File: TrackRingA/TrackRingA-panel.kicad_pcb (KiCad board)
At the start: 2 copper layers, 81 x 81 mm, 350 parts, among them J1 Conn_01x04, U1 TLV493D-A1B6, U2 LIS2DTW12

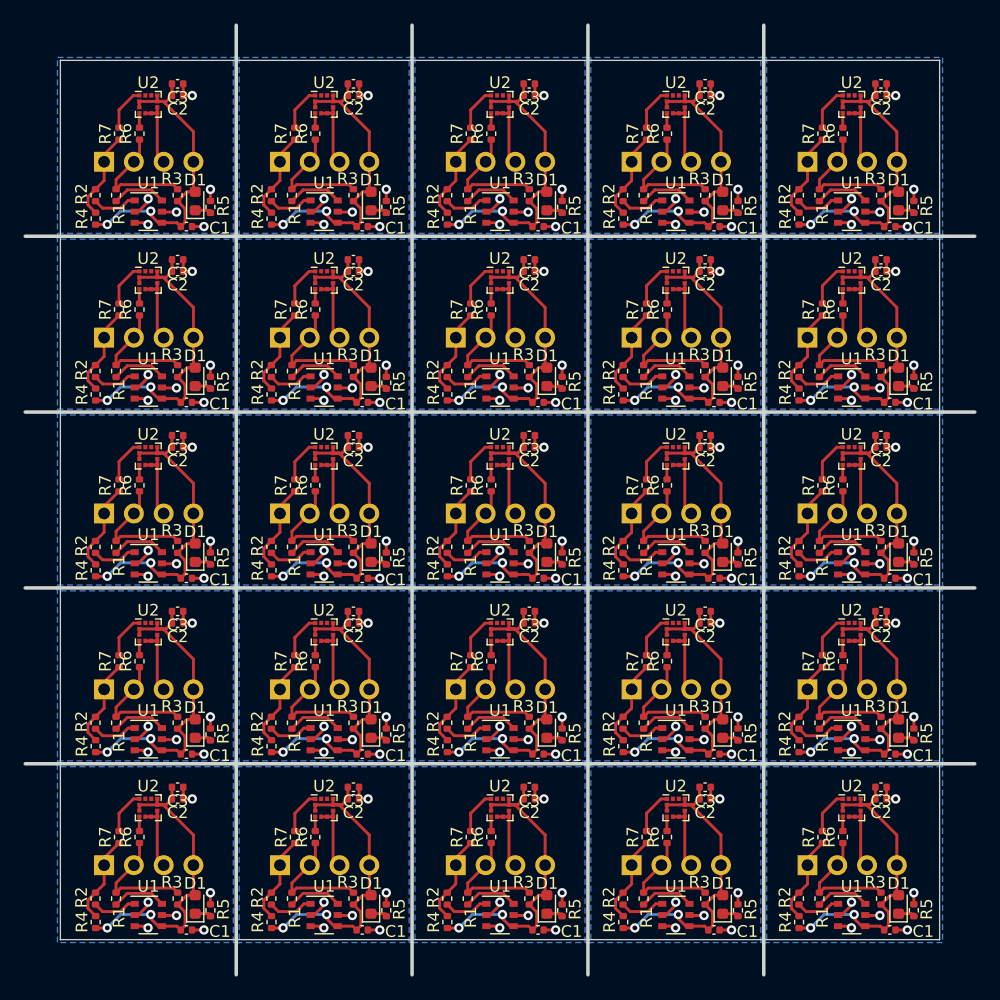
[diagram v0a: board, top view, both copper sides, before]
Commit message: Finished BusChain1.1 and added power daisy-chaining option
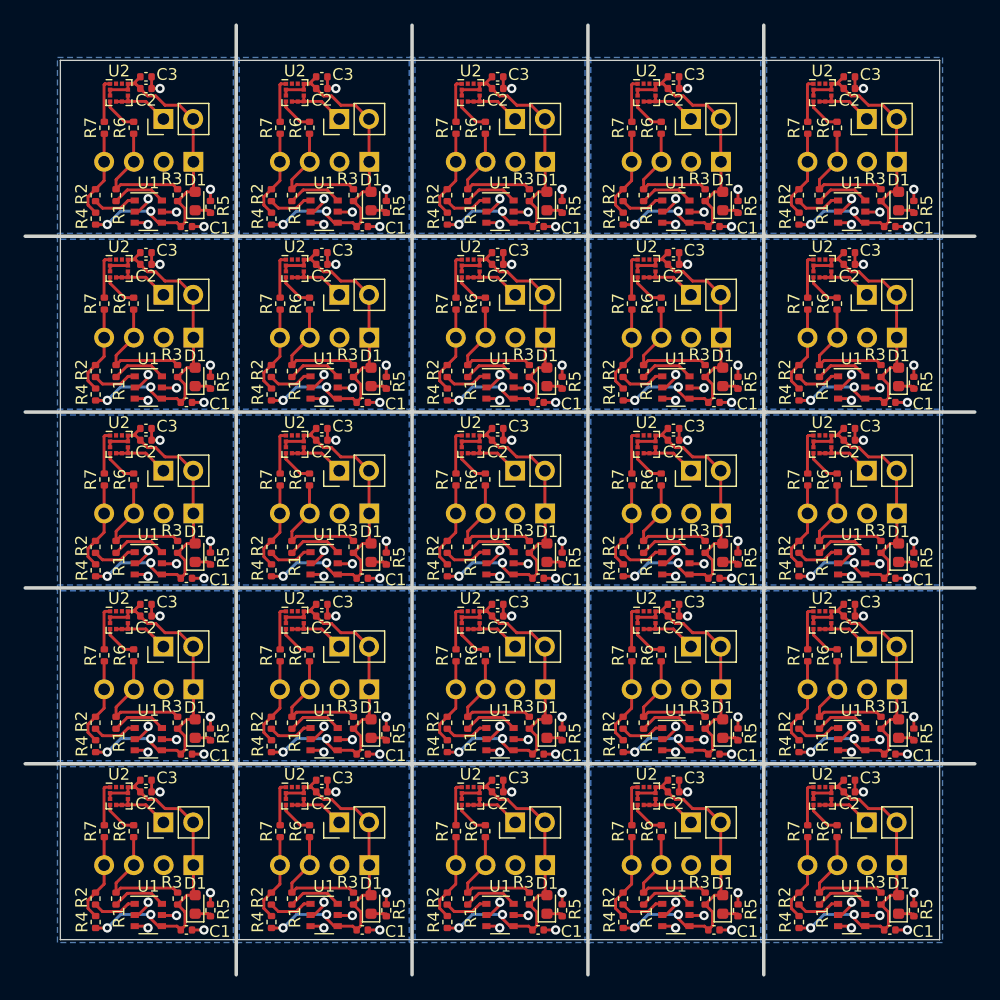
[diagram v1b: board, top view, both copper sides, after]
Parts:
- removed the C2 at (121.0, 53.0)
- removed the C2 at (166.0, 53.0)
- removed the C2 at (136.0, 23.0)
- removed the C2 at (166.0, 68.0)
- removed the C2 at (181.0, 68.0)
- removed the C2 at (136.0, 53.0)
- removed the C2 at (151.0, 23.0)
- removed the C2 at (166.0, 38.0)
- removed the C2 at (166.0, 83.0)
- removed the C2 at (151.0, 68.0)
- removed the C2 at (181.0, 38.0)
- removed the C2 at (181.0, 23.0)
- removed the C2 at (121.0, 38.0)
- removed the C2 at (151.0, 83.0)
- removed the C2 at (136.0, 38.0)
- removed the C2 at (121.0, 68.0)
- removed the C2 at (136.0, 83.0)
- removed the C2 at (151.0, 53.0)
- removed the C2 at (166.0, 23.0)
- removed the C2 at (181.0, 83.0)
- removed the C2 at (136.0, 68.0)
- removed the C2 at (151.0, 38.0)
- removed the C2 at (121.0, 83.0)
- removed the C2 at (181.0, 53.0)
- removed the C3 at (181.0, 22.0)
- removed the C3 at (166.0, 37.0)
- removed the C3 at (121.0, 67.0)
- removed the C3 at (136.0, 82.0)
- removed the C3 at (181.0, 67.0)
- removed the C3 at (136.0, 52.0)
- removed the C3 at (121.0, 22.0)
- removed the C3 at (136.0, 67.0)
- removed the C3 at (151.0, 37.0)
- removed the C3 at (151.0, 82.0)
- removed the C3 at (121.0, 82.0)
- removed the C3 at (181.0, 82.0)
- removed the C3 at (121.0, 37.0)
- removed the C3 at (151.0, 22.0)
- removed the C3 at (166.0, 52.0)
- removed the C3 at (121.0, 52.0)
- removed the C3 at (166.0, 82.0)
- removed the C3 at (181.0, 37.0)
- removed the C3 at (151.0, 52.0)
- removed the C3 at (181.0, 52.0)
- removed the C3 at (166.0, 67.0)
- removed the C3 at (136.0, 37.0)
- removed the C3 at (151.0, 67.0)
- removed the C3 at (136.0, 22.0)
- removed the J1 at (174.7, 58.6)
- removed the J1 at (144.7, 43.6)
- removed the J1 at (144.7, 28.6)
- removed the J1 at (129.7, 73.7)
- removed the J1 at (159.7, 43.6)
- removed the J1 at (114.7, 88.7)
- removed the J1 at (174.7, 88.7)
- removed the J1 at (174.7, 43.6)
- removed the J1 at (144.7, 88.7)
- removed the J1 at (159.7, 88.7)
- removed the J1 at (144.7, 73.7)
- removed the J1 at (159.7, 28.6)
- removed the J1 at (129.7, 28.6)
- removed the J1 at (114.7, 28.6)
- removed the J1 at (159.7, 73.7)
- removed the J1 at (144.7, 58.6)
- removed the J1 at (114.7, 43.6)
- removed the J1 at (114.7, 58.6)
- removed the J1 at (159.7, 58.6)
- removed the J1 at (129.7, 58.6)
- removed the J1 at (114.7, 73.7)
- removed the J1 at (174.7, 73.7)
- removed the J1 at (129.7, 43.6)
- removed the J1 at (129.7, 88.7)
- removed the J1 at (174.7, 28.6)
- removed the R6 at (177.8, 26.2)
- removed the R6 at (162.8, 86.2)
- removed the R6 at (117.8, 71.2)
- removed the R6 at (132.8, 71.2)
- removed the R6 at (162.8, 71.2)
- removed the R6 at (147.8, 86.2)
- removed the R6 at (177.8, 71.2)
- removed the R6 at (147.8, 26.2)
- removed the R6 at (132.8, 41.2)
- removed the R6 at (147.8, 71.2)
- removed the R6 at (132.8, 86.2)
- removed the R6 at (132.8, 56.2)
- removed the R6 at (177.8, 86.2)
- removed the R6 at (147.8, 56.2)
- removed the R6 at (162.8, 26.2)
- removed the R6 at (162.8, 56.2)
- removed the R6 at (117.8, 56.2)
- removed the R6 at (117.8, 86.2)
- removed the R6 at (177.8, 41.2)
- removed the R6 at (147.8, 41.2)
- removed the R6 at (117.8, 26.2)
- removed the R6 at (177.8, 56.2)
- removed the R6 at (117.8, 41.2)
- removed the R6 at (162.8, 41.2)
- removed the R7 at (131.0, 86.2)
- removed the R7 at (176.0, 71.2)
- removed the R7 at (176.0, 41.2)
- removed the R7 at (131.0, 71.2)
- removed the R7 at (161.0, 86.2)
- removed the R7 at (161.0, 26.2)
- removed the R7 at (161.0, 56.2)
- removed the R7 at (116.0, 26.2)
- removed the R7 at (146.0, 56.2)
- removed the R7 at (146.0, 86.2)
- removed the R7 at (131.0, 41.2)
- removed the R7 at (176.0, 86.2)
- removed the R7 at (131.0, 56.2)
- removed the R7 at (161.0, 41.2)
- removed the R7 at (176.0, 56.2)
- removed the R7 at (116.0, 86.2)
- removed the R7 at (116.0, 71.2)
- removed the R7 at (146.0, 41.2)
- removed the R7 at (146.0, 71.2)
- removed the R7 at (116.0, 41.2)
- removed the R7 at (116.0, 56.2)
- removed the R7 at (146.0, 26.2)
- removed the R7 at (161.0, 71.2)
- removed the R7 at (176.0, 26.2)
- removed the U2 at (118.5, 83.8)
- removed the U2 at (163.5, 68.8)
- removed the U2 at (133.5, 83.8)
- removed the U2 at (163.5, 38.8)
- removed the U2 at (148.5, 38.8)
- removed the U2 at (163.5, 23.8)
- removed the U2 at (133.5, 38.8)
- removed the U2 at (118.5, 68.8)
- removed the U2 at (148.5, 83.8)
- removed the U2 at (118.5, 38.8)
- removed the U2 at (118.5, 53.8)
- removed the U2 at (163.5, 83.8)
- removed the U2 at (133.5, 53.8)
- removed the U2 at (148.5, 53.8)
- removed the U2 at (178.5, 23.8)
- removed the U2 at (178.5, 68.8)
- removed the U2 at (148.5, 23.8)
- removed the U2 at (178.5, 38.8)
- removed the U2 at (148.5, 68.8)
- removed the U2 at (178.5, 83.8)
- removed the U2 at (133.5, 68.8)
- removed the U2 at (163.5, 53.8)
- removed the U2 at (178.5, 53.8)
- removed the U2 at (133.5, 23.8)
- added C2: 0.1uF, Capacitor_SMD:C_0402_1005Metric, F.Cu at (118.3, 67.4)
- added C2: 0.1uF, Capacitor_SMD:C_0402_1005Metric, F.Cu at (148.3, 37.4)
- added C2: 0.1uF, Capacitor_SMD:C_0402_1005Metric, F.Cu at (163.3, 82.4)
- added C2: 0.1uF, Capacitor_SMD:C_0402_1005Metric, F.Cu at (133.3, 37.4)
- added C2: 0.1uF, Capacitor_SMD:C_0402_1005Metric, F.Cu at (163.3, 67.4)
- added C2: 0.1uF, Capacitor_SMD:C_0402_1005Metric, F.Cu at (148.3, 67.4)
- added C2: 0.1uF, Capacitor_SMD:C_0402_1005Metric, F.Cu at (178.3, 67.4)
- added C2: 0.1uF, Capacitor_SMD:C_0402_1005Metric, F.Cu at (178.3, 37.4)
- added C2: 0.1uF, Capacitor_SMD:C_0402_1005Metric, F.Cu at (178.3, 22.4)
- added C2: 0.1uF, Capacitor_SMD:C_0402_1005Metric, F.Cu at (178.3, 52.4)
- added C2: 0.1uF, Capacitor_SMD:C_0402_1005Metric, F.Cu at (163.3, 37.4)
- added C2: 0.1uF, Capacitor_SMD:C_0402_1005Metric, F.Cu at (163.3, 22.4)
- added C2: 0.1uF, Capacitor_SMD:C_0402_1005Metric, F.Cu at (163.3, 52.4)
- added C2: 0.1uF, Capacitor_SMD:C_0402_1005Metric, F.Cu at (133.3, 82.4)
- added C2: 0.1uF, Capacitor_SMD:C_0402_1005Metric, F.Cu at (118.3, 52.4)
- added C2: 0.1uF, Capacitor_SMD:C_0402_1005Metric, F.Cu at (133.3, 22.4)
- added C2: 0.1uF, Capacitor_SMD:C_0402_1005Metric, F.Cu at (148.3, 82.4)
- added C2: 0.1uF, Capacitor_SMD:C_0402_1005Metric, F.Cu at (178.3, 82.4)
- added C2: 0.1uF, Capacitor_SMD:C_0402_1005Metric, F.Cu at (133.3, 67.4)
- added C2: 0.1uF, Capacitor_SMD:C_0402_1005Metric, F.Cu at (133.3, 52.4)
- added C2: 0.1uF, Capacitor_SMD:C_0402_1005Metric, F.Cu at (118.3, 22.4)
- added C2: 0.1uF, Capacitor_SMD:C_0402_1005Metric, F.Cu at (118.3, 37.4)
- added C2: 0.1uF, Capacitor_SMD:C_0402_1005Metric, F.Cu at (148.3, 52.4)
- added C2: 0.1uF, Capacitor_SMD:C_0402_1005Metric, F.Cu at (118.3, 82.4)
- added C3: 0.1uF, Capacitor_SMD:C_0402_1005Metric, F.Cu at (163.3, 66.4)
- added C3: 0.1uF, Capacitor_SMD:C_0402_1005Metric, F.Cu at (118.3, 36.4)
- added C3: 0.1uF, Capacitor_SMD:C_0402_1005Metric, F.Cu at (178.3, 36.4)
- added C3: 0.1uF, Capacitor_SMD:C_0402_1005Metric, F.Cu at (133.3, 51.4)
- added C3: 0.1uF, Capacitor_SMD:C_0402_1005Metric, F.Cu at (118.3, 21.4)
- added C3: 0.1uF, Capacitor_SMD:C_0402_1005Metric, F.Cu at (163.3, 51.4)
- added C3: 0.1uF, Capacitor_SMD:C_0402_1005Metric, F.Cu at (178.3, 51.4)
- added C3: 0.1uF, Capacitor_SMD:C_0402_1005Metric, F.Cu at (148.3, 66.4)
- added C3: 0.1uF, Capacitor_SMD:C_0402_1005Metric, F.Cu at (178.3, 21.4)
- added C3: 0.1uF, Capacitor_SMD:C_0402_1005Metric, F.Cu at (178.3, 81.4)
- added C3: 0.1uF, Capacitor_SMD:C_0402_1005Metric, F.Cu at (133.3, 81.4)
- added C3: 0.1uF, Capacitor_SMD:C_0402_1005Metric, F.Cu at (148.3, 21.4)
- added C3: 0.1uF, Capacitor_SMD:C_0402_1005Metric, F.Cu at (163.3, 21.4)
- added C3: 0.1uF, Capacitor_SMD:C_0402_1005Metric, F.Cu at (118.3, 51.4)
- added C3: 0.1uF, Capacitor_SMD:C_0402_1005Metric, F.Cu at (118.3, 81.4)
- added C3: 0.1uF, Capacitor_SMD:C_0402_1005Metric, F.Cu at (178.3, 66.4)
- added C3: 0.1uF, Capacitor_SMD:C_0402_1005Metric, F.Cu at (163.3, 36.4)
- added C3: 0.1uF, Capacitor_SMD:C_0402_1005Metric, F.Cu at (148.3, 81.4)
- added C3: 0.1uF, Capacitor_SMD:C_0402_1005Metric, F.Cu at (133.3, 66.4)
- added C3: 0.1uF, Capacitor_SMD:C_0402_1005Metric, F.Cu at (118.3, 66.4)
- added C3: 0.1uF, Capacitor_SMD:C_0402_1005Metric, F.Cu at (148.3, 36.4)
- added C3: 0.1uF, Capacitor_SMD:C_0402_1005Metric, F.Cu at (133.3, 21.4)
- added C3: 0.1uF, Capacitor_SMD:C_0402_1005Metric, F.Cu at (148.3, 51.4)
- added C3: 0.1uF, Capacitor_SMD:C_0402_1005Metric, F.Cu at (163.3, 81.4)
- added J1: Conn_01x04, Connector_PinHeader_2.54mm:PinHeader_1x04_P2.54mm_Vertical, B.Cu at (137.3, 43.6)
- added J1: Conn_01x04, Connector_PinHeader_2.54mm:PinHeader_1x04_P2.54mm_Vertical, B.Cu at (167.3, 43.6)
- added J1: Conn_01x04, Connector_PinHeader_2.54mm:PinHeader_1x04_P2.54mm_Vertical, B.Cu at (182.3, 28.6)
- added J1: Conn_01x04, Connector_PinHeader_2.54mm:PinHeader_1x04_P2.54mm_Vertical, B.Cu at (152.3, 28.6)
- added J1: Conn_01x04, Connector_PinHeader_2.54mm:PinHeader_1x04_P2.54mm_Vertical, B.Cu at (152.3, 58.6)
- added J1: Conn_01x04, Connector_PinHeader_2.54mm:PinHeader_1x04_P2.54mm_Vertical, B.Cu at (152.3, 43.6)
- added J1: Conn_01x04, Connector_PinHeader_2.54mm:PinHeader_1x04_P2.54mm_Vertical, B.Cu at (137.3, 88.7)
- added J1: Conn_01x04, Connector_PinHeader_2.54mm:PinHeader_1x04_P2.54mm_Vertical, B.Cu at (167.3, 88.7)
- added J1: Conn_01x04, Connector_PinHeader_2.54mm:PinHeader_1x04_P2.54mm_Vertical, B.Cu at (122.3, 58.6)
- added J1: Conn_01x04, Connector_PinHeader_2.54mm:PinHeader_1x04_P2.54mm_Vertical, B.Cu at (182.3, 58.6)
- added J1: Conn_01x04, Connector_PinHeader_2.54mm:PinHeader_1x04_P2.54mm_Vertical, B.Cu at (122.3, 28.6)
- added J1: Conn_01x04, Connector_PinHeader_2.54mm:PinHeader_1x04_P2.54mm_Vertical, B.Cu at (182.3, 43.6)
- added J1: Conn_01x04, Connector_PinHeader_2.54mm:PinHeader_1x04_P2.54mm_Vertical, B.Cu at (167.3, 73.7)
- added J1: Conn_01x04, Connector_PinHeader_2.54mm:PinHeader_1x04_P2.54mm_Vertical, B.Cu at (137.3, 73.7)
- added J1: Conn_01x04, Connector_PinHeader_2.54mm:PinHeader_1x04_P2.54mm_Vertical, B.Cu at (182.3, 88.7)
- added J1: Conn_01x04, Connector_PinHeader_2.54mm:PinHeader_1x04_P2.54mm_Vertical, B.Cu at (137.3, 28.6)
- added J1: Conn_01x04, Connector_PinHeader_2.54mm:PinHeader_1x04_P2.54mm_Vertical, B.Cu at (137.3, 58.6)
- added J1: Conn_01x04, Connector_PinHeader_2.54mm:PinHeader_1x04_P2.54mm_Vertical, B.Cu at (167.3, 28.6)
- added J1: Conn_01x04, Connector_PinHeader_2.54mm:PinHeader_1x04_P2.54mm_Vertical, B.Cu at (122.3, 43.6)
- added J1: Conn_01x04, Connector_PinHeader_2.54mm:PinHeader_1x04_P2.54mm_Vertical, B.Cu at (122.3, 73.7)
- added J1: Conn_01x04, Connector_PinHeader_2.54mm:PinHeader_1x04_P2.54mm_Vertical, B.Cu at (152.3, 88.7)
- added J1: Conn_01x04, Connector_PinHeader_2.54mm:PinHeader_1x04_P2.54mm_Vertical, B.Cu at (152.3, 73.7)
- added J1: Conn_01x04, Connector_PinHeader_2.54mm:PinHeader_1x04_P2.54mm_Vertical, B.Cu at (122.3, 88.7)
- added J1: Conn_01x04, Connector_PinHeader_2.54mm:PinHeader_1x04_P2.54mm_Vertical, B.Cu at (167.3, 58.6)
- added J1: Conn_01x04, Connector_PinHeader_2.54mm:PinHeader_1x04_P2.54mm_Vertical, B.Cu at (182.3, 73.7)
- added J2: Conn_01x02, Connector_PinHeader_2.54mm:PinHeader_1x02_P2.54mm_Vertical, F.Cu at (164.8, 40.0)
- added J2: Conn_01x02, Connector_PinHeader_2.54mm:PinHeader_1x02_P2.54mm_Vertical, F.Cu at (134.8, 85.0)
- added J2: Conn_01x02, Connector_PinHeader_2.54mm:PinHeader_1x02_P2.54mm_Vertical, F.Cu at (119.8, 55.0)
- added J2: Conn_01x02, Connector_PinHeader_2.54mm:PinHeader_1x02_P2.54mm_Vertical, F.Cu at (149.8, 85.0)
- added J2: Conn_01x02, Connector_PinHeader_2.54mm:PinHeader_1x02_P2.54mm_Vertical, F.Cu at (179.8, 85.0)
- added J2: Conn_01x02, Connector_PinHeader_2.54mm:PinHeader_1x02_P2.54mm_Vertical, F.Cu at (149.8, 25.0)
- added J2: Conn_01x02, Connector_PinHeader_2.54mm:PinHeader_1x02_P2.54mm_Vertical, F.Cu at (134.8, 40.0)
- added J2: Conn_01x02, Connector_PinHeader_2.54mm:PinHeader_1x02_P2.54mm_Vertical, F.Cu at (164.8, 25.0)
- added J2: Conn_01x02, Connector_PinHeader_2.54mm:PinHeader_1x02_P2.54mm_Vertical, F.Cu at (134.8, 70.0)
- added J2: Conn_01x02, Connector_PinHeader_2.54mm:PinHeader_1x02_P2.54mm_Vertical, F.Cu at (134.8, 25.0)
- added J2: Conn_01x02, Connector_PinHeader_2.54mm:PinHeader_1x02_P2.54mm_Vertical, F.Cu at (179.8, 40.0)
- added J2: Conn_01x02, Connector_PinHeader_2.54mm:PinHeader_1x02_P2.54mm_Vertical, F.Cu at (179.8, 70.0)
- added J2: Conn_01x02, Connector_PinHeader_2.54mm:PinHeader_1x02_P2.54mm_Vertical, F.Cu at (149.8, 40.0)
- added J2: Conn_01x02, Connector_PinHeader_2.54mm:PinHeader_1x02_P2.54mm_Vertical, F.Cu at (119.8, 70.0)
- added J2: Conn_01x02, Connector_PinHeader_2.54mm:PinHeader_1x02_P2.54mm_Vertical, F.Cu at (164.8, 85.0)
- added J2: Conn_01x02, Connector_PinHeader_2.54mm:PinHeader_1x02_P2.54mm_Vertical, F.Cu at (149.8, 70.0)
- added J2: Conn_01x02, Connector_PinHeader_2.54mm:PinHeader_1x02_P2.54mm_Vertical, F.Cu at (179.8, 25.0)
- added J2: Conn_01x02, Connector_PinHeader_2.54mm:PinHeader_1x02_P2.54mm_Vertical, F.Cu at (119.8, 25.0)
- added J2: Conn_01x02, Connector_PinHeader_2.54mm:PinHeader_1x02_P2.54mm_Vertical, F.Cu at (164.8, 55.0)
- added J2: Conn_01x02, Connector_PinHeader_2.54mm:PinHeader_1x02_P2.54mm_Vertical, F.Cu at (179.8, 55.0)
- added J2: Conn_01x02, Connector_PinHeader_2.54mm:PinHeader_1x02_P2.54mm_Vertical, F.Cu at (134.8, 55.0)
- added J2: Conn_01x02, Connector_PinHeader_2.54mm:PinHeader_1x02_P2.54mm_Vertical, F.Cu at (119.8, 40.0)
- added J2: Conn_01x02, Connector_PinHeader_2.54mm:PinHeader_1x02_P2.54mm_Vertical, F.Cu at (149.8, 55.0)
- added J2: Conn_01x02, Connector_PinHeader_2.54mm:PinHeader_1x02_P2.54mm_Vertical, F.Cu at (164.8, 70.0)
- added J2: Conn_01x02, Connector_PinHeader_2.54mm:PinHeader_1x02_P2.54mm_Vertical, F.Cu at (119.8, 85.0)
- added R6: 100, Resistor_SMD:R_0402_1005Metric, F.Cu at (162.2, 55.8)
- added R6: 100, Resistor_SMD:R_0402_1005Metric, F.Cu at (177.2, 40.8)
- added R6: 100, Resistor_SMD:R_0402_1005Metric, F.Cu at (177.2, 55.8)
- added R6: 100, Resistor_SMD:R_0402_1005Metric, F.Cu at (162.2, 25.8)
- added R6: 100, Resistor_SMD:R_0402_1005Metric, F.Cu at (177.2, 85.8)
- added R6: 100, Resistor_SMD:R_0402_1005Metric, F.Cu at (147.2, 25.8)
- added R6: 100, Resistor_SMD:R_0402_1005Metric, F.Cu at (147.2, 40.8)
- added R6: 100, Resistor_SMD:R_0402_1005Metric, F.Cu at (117.2, 85.8)
- added R6: 100, Resistor_SMD:R_0402_1005Metric, F.Cu at (162.2, 40.8)
- added R6: 100, Resistor_SMD:R_0402_1005Metric, F.Cu at (117.2, 55.8)
- added R6: 100, Resistor_SMD:R_0402_1005Metric, F.Cu at (162.2, 70.8)
- added R6: 100, Resistor_SMD:R_0402_1005Metric, F.Cu at (132.2, 85.8)
- added R6: 100, Resistor_SMD:R_0402_1005Metric, F.Cu at (132.2, 40.8)
- added R6: 100, Resistor_SMD:R_0402_1005Metric, F.Cu at (177.2, 25.8)
- added R6: 100, Resistor_SMD:R_0402_1005Metric, F.Cu at (162.2, 85.8)
- added R6: 100, Resistor_SMD:R_0402_1005Metric, F.Cu at (177.2, 70.8)
- added R6: 100, Resistor_SMD:R_0402_1005Metric, F.Cu at (147.2, 70.8)
- added R6: 100, Resistor_SMD:R_0402_1005Metric, F.Cu at (117.2, 70.8)
- added R6: 100, Resistor_SMD:R_0402_1005Metric, F.Cu at (117.2, 40.8)
- added R6: 100, Resistor_SMD:R_0402_1005Metric, F.Cu at (147.2, 55.8)
- added R6: 100, Resistor_SMD:R_0402_1005Metric, F.Cu at (117.2, 25.8)
- added R6: 100, Resistor_SMD:R_0402_1005Metric, F.Cu at (147.2, 85.8)
- added R6: 100, Resistor_SMD:R_0402_1005Metric, F.Cu at (132.2, 70.8)
- added R6: 100, Resistor_SMD:R_0402_1005Metric, F.Cu at (132.2, 55.8)
- added R7: 100, Resistor_SMD:R_0402_1005Metric, F.Cu at (129.8, 70.8)
- added R7: 100, Resistor_SMD:R_0402_1005Metric, F.Cu at (129.8, 25.8)
- added R7: 100, Resistor_SMD:R_0402_1005Metric, F.Cu at (144.8, 25.8)
- added R7: 100, Resistor_SMD:R_0402_1005Metric, F.Cu at (129.8, 40.8)
- added R7: 100, Resistor_SMD:R_0402_1005Metric, F.Cu at (174.8, 70.8)
- added R7: 100, Resistor_SMD:R_0402_1005Metric, F.Cu at (159.8, 70.8)
- added R7: 100, Resistor_SMD:R_0402_1005Metric, F.Cu at (144.8, 55.8)
- added R7: 100, Resistor_SMD:R_0402_1005Metric, F.Cu at (114.8, 70.8)
- added R7: 100, Resistor_SMD:R_0402_1005Metric, F.Cu at (144.8, 40.8)
- added R7: 100, Resistor_SMD:R_0402_1005Metric, F.Cu at (129.8, 85.8)
- added R7: 100, Resistor_SMD:R_0402_1005Metric, F.Cu at (159.8, 55.8)
- added R7: 100, Resistor_SMD:R_0402_1005Metric, F.Cu at (129.8, 55.8)
- added R7: 100, Resistor_SMD:R_0402_1005Metric, F.Cu at (174.8, 40.8)
- added R7: 100, Resistor_SMD:R_0402_1005Metric, F.Cu at (114.8, 40.8)
- added R7: 100, Resistor_SMD:R_0402_1005Metric, F.Cu at (174.8, 25.8)
- added R7: 100, Resistor_SMD:R_0402_1005Metric, F.Cu at (159.8, 85.8)
- added R7: 100, Resistor_SMD:R_0402_1005Metric, F.Cu at (114.8, 55.8)
- added R7: 100, Resistor_SMD:R_0402_1005Metric, F.Cu at (144.8, 70.8)
- added R7: 100, Resistor_SMD:R_0402_1005Metric, F.Cu at (159.8, 40.8)
- added R7: 100, Resistor_SMD:R_0402_1005Metric, F.Cu at (174.8, 85.8)
- added R7: 100, Resistor_SMD:R_0402_1005Metric, F.Cu at (114.8, 85.8)
- added R7: 100, Resistor_SMD:R_0402_1005Metric, F.Cu at (144.8, 85.8)
- added R7: 100, Resistor_SMD:R_0402_1005Metric, F.Cu at (174.8, 55.8)
- added R7: 100, Resistor_SMD:R_0402_1005Metric, F.Cu at (114.8, 25.8)
- added U2: LIS2DTW12, Package_LGA:LGA-12_2x2mm_P0.5mm, F.Cu at (161.0, 82.8)
- added U2: LIS2DTW12, Package_LGA:LGA-12_2x2mm_P0.5mm, F.Cu at (131.0, 37.8)
- added U2: LIS2DTW12, Package_LGA:LGA-12_2x2mm_P0.5mm, F.Cu at (131.0, 22.8)
- added U2: LIS2DTW12, Package_LGA:LGA-12_2x2mm_P0.5mm, F.Cu at (161.0, 22.8)
- added U2: LIS2DTW12, Package_LGA:LGA-12_2x2mm_P0.5mm, F.Cu at (116.0, 82.8)
- added U2: LIS2DTW12, Package_LGA:LGA-12_2x2mm_P0.5mm, F.Cu at (146.0, 67.8)
- added U2: LIS2DTW12, Package_LGA:LGA-12_2x2mm_P0.5mm, F.Cu at (161.0, 52.8)
- added U2: LIS2DTW12, Package_LGA:LGA-12_2x2mm_P0.5mm, F.Cu at (176.0, 52.8)
- added U2: LIS2DTW12, Package_LGA:LGA-12_2x2mm_P0.5mm, F.Cu at (176.0, 67.8)
- added U2: LIS2DTW12, Package_LGA:LGA-12_2x2mm_P0.5mm, F.Cu at (131.0, 67.8)
- added U2: LIS2DTW12, Package_LGA:LGA-12_2x2mm_P0.5mm, F.Cu at (131.0, 82.8)
- added U2: LIS2DTW12, Package_LGA:LGA-12_2x2mm_P0.5mm, F.Cu at (161.0, 37.8)
- added U2: LIS2DTW12, Package_LGA:LGA-12_2x2mm_P0.5mm, F.Cu at (176.0, 82.8)
- added U2: LIS2DTW12, Package_LGA:LGA-12_2x2mm_P0.5mm, F.Cu at (116.0, 67.8)
- added U2: LIS2DTW12, Package_LGA:LGA-12_2x2mm_P0.5mm, F.Cu at (116.0, 22.8)
- added U2: LIS2DTW12, Package_LGA:LGA-12_2x2mm_P0.5mm, F.Cu at (116.0, 52.8)
- added U2: LIS2DTW12, Package_LGA:LGA-12_2x2mm_P0.5mm, F.Cu at (116.0, 37.8)
- added U2: LIS2DTW12, Package_LGA:LGA-12_2x2mm_P0.5mm, F.Cu at (146.0, 37.8)
- added U2: LIS2DTW12, Package_LGA:LGA-12_2x2mm_P0.5mm, F.Cu at (176.0, 37.8)
- added U2: LIS2DTW12, Package_LGA:LGA-12_2x2mm_P0.5mm, F.Cu at (146.0, 52.8)
- added U2: LIS2DTW12, Package_LGA:LGA-12_2x2mm_P0.5mm, F.Cu at (146.0, 82.8)
- added U2: LIS2DTW12, Package_LGA:LGA-12_2x2mm_P0.5mm, F.Cu at (161.0, 67.8)
- added U2: LIS2DTW12, Package_LGA:LGA-12_2x2mm_P0.5mm, F.Cu at (131.0, 52.8)
- added U2: LIS2DTW12, Package_LGA:LGA-12_2x2mm_P0.5mm, F.Cu at (176.0, 22.8)
- moved R3 60.0 mm to (181.0, 91.5)
- moved R3 60.0 mm to (181.0, 31.5)
- moved R1 45.0 mm to (115.8, 31.5)
- moved R1 45.0 mm to (160.8, 31.5)
- moved C3 35.7 mm to (133.3, 36.4)
- moved R7 28.8 mm to (159.8, 25.8)
- moved U2 27.5 mm to (146.0, 22.8)
- moved C2 27.3 mm to (148.3, 22.4)
- moved D1 15.0 mm to (137.5, 32.0)
- moved D1 15.0 mm to (122.5, 32.0)
- moved R2 15.0 mm to (114.0, 31.5)
- moved R2 15.0 mm to (129.0, 31.5)
- moved R4 15.0 mm to (159.0, 33.5)
- moved R4 15.0 mm to (174.0, 33.5)
- moved U1 15.0 mm to (118.5, 47.9)
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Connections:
- C2 pad 1: Board_0-GND -> Board_2-GND
- C2 pad 2: Board_0-/VCC -> Board_2-/VCC
- C3 pad 1: Board_3-GND -> Board_6-GND
- C3 pad 2: Board_3-/VCC -> Board_6-/VCC
- D1 pad 1: Board_0-Net-(D1-K) -> Board_1-Net-(D1-K)
- D1 pad 2: Board_0-/VCC -> Board_1-/VCC
- D1 pad 1: Board_1-Net-(D1-K) -> Board_0-Net-(D1-K)
- D1 pad 2: Board_1-/VCC -> Board_0-/VCC
- R1 pad 1: Board_3-/SDA -> Board_0-/SDA
- R1 pad 2: Board_3-Net-(U1-SDA) -> Board_0-Net-(U1-SDA)
- R1 pad 1: Board_0-/SDA -> Board_3-/SDA
- R1 pad 2: Board_0-Net-(U1-SDA) -> Board_3-Net-(U1-SDA)
- R2 pad 1: Board_1-/SCL -> Board_0-/SCL
- R2 pad 2: Board_1-Net-(U1-SCL) -> Board_0-Net-(U1-SCL)
- R2 pad 1: Board_0-/SCL -> Board_1-/SCL
- R2 pad 2: Board_0-Net-(U1-SCL) -> Board_1-Net-(U1-SCL)
- R3 pad 1: Board_4-/VCC -> Board_24-/VCC
- R3 pad 2: Board_4-/SDA -> Board_24-/SDA
- R3 pad 1: Board_24-/VCC -> Board_4-/VCC
- R3 pad 2: Board_24-/SDA -> Board_4-/SDA
- R4 pad 1: Board_4-/VCC -> Board_3-/VCC
- R4 pad 2: Board_4-/SCL -> Board_3-/SCL
- R4 pad 1: Board_3-/VCC -> Board_4-/VCC
- R4 pad 2: Board_3-/SCL -> Board_4-/SCL
- R7 pad 1: Board_1-/SCL -> Board_3-/SCL
- R7 pad 2: Board_1-Net-(U2-SCL/SPC) -> Board_3-Net-(U2-SCL/SPC)
- U1 pad 1: Board_0-Net-(U1-SCL) -> Board_5-Net-(U1-SCL)
- U1 pad 2: Board_0-GND -> Board_5-GND
- U1 pad 3: Board_0-GND -> Board_5-GND
- U1 pad 4: Board_0-/VCC -> Board_5-/VCC
- U1 pad 5: Board_0-GND -> Board_5-GND
- U1 pad 6: Board_0-Net-(U1-SDA) -> Board_5-Net-(U1-SDA)
- U1 pad 1: Board_5-Net-(U1-SCL) -> Board_0-Net-(U1-SCL)
- U1 pad 2: Board_5-GND -> Board_0-GND
- U1 pad 3: Board_5-GND -> Board_0-GND
- U1 pad 4: Board_5-/VCC -> Board_0-/VCC
- U1 pad 5: Board_5-GND -> Board_0-GND
- U1 pad 6: Board_5-Net-(U1-SDA) -> Board_0-Net-(U1-SDA)
- U2 pad 1: Board_0-Net-(U2-SCL/SPC) -> Board_2-Net-(U2-SCL/SPC)
- U2 pad 10: Board_0-/VCC -> Board_2-/VCC
- U2 pad 11: Board_0-unconnected-(U2-INT2-Pad11) -> Board_2-unconnected-(U2-INT2-Pad11)
- U2 pad 12: Board_0-unconnected-(U2-INT1-Pad12) -> Board_2-unconnected-(U2-INT1-Pad12)
- U2 pad 2: Board_0-/VCC -> Board_2-/VCC
- U2 pad 3: Board_0-/VCC -> Board_2-/VCC
- U2 pad 4: Board_0-Net-(U2-SDA/SDI/SDO) -> Board_2-Net-(U2-SDA/SDI/SDO)
- U2 pad 5: Board_0-GND -> Board_2-GND
- U2 pad 6: Board_0-GND -> Board_2-GND
- U2 pad 7: Board_0-GND -> Board_2-GND
- U2 pad 8: Board_0-GND -> Board_2-GND
- U2 pad 9: Board_0-/VCC -> Board_2-/VCC
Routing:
- net Board_5-/VCC: track 27.2 -> 29.8 mm
- net Board_10-/VCC: track 27.2 -> 29.8 mm
- net Board_0-/VCC: track 27.2 -> 29.8 mm
- net Board_20-/VCC: track 27.2 -> 29.8 mm
- net Board_15-/VCC: track 27.2 -> 29.8 mm
- net Board_4-/VCC: track 27.2 -> 29.8 mm
- net Board_13-/VCC: track 27.2 -> 29.8 mm
- net Board_9-/VCC: track 27.2 -> 29.8 mm
- net Board_8-/VCC: track 27.2 -> 29.8 mm
- net Board_7-/VCC: track 27.2 -> 29.8 mm
- net Board_6-/VCC: track 27.2 -> 29.8 mm
- net Board_2-/VCC: track 27.2 -> 29.8 mm
- net Board_14-/VCC: track 27.2 -> 29.8 mm
- net Board_12-/VCC: track 27.2 -> 29.8 mm
- net Board_11-/VCC: track 27.2 -> 29.8 mm
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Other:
- board text added: "TrackNode 1.1"
- board text removed: "TrackRing 1.0"
